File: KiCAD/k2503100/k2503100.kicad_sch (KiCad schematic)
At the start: 0 parts

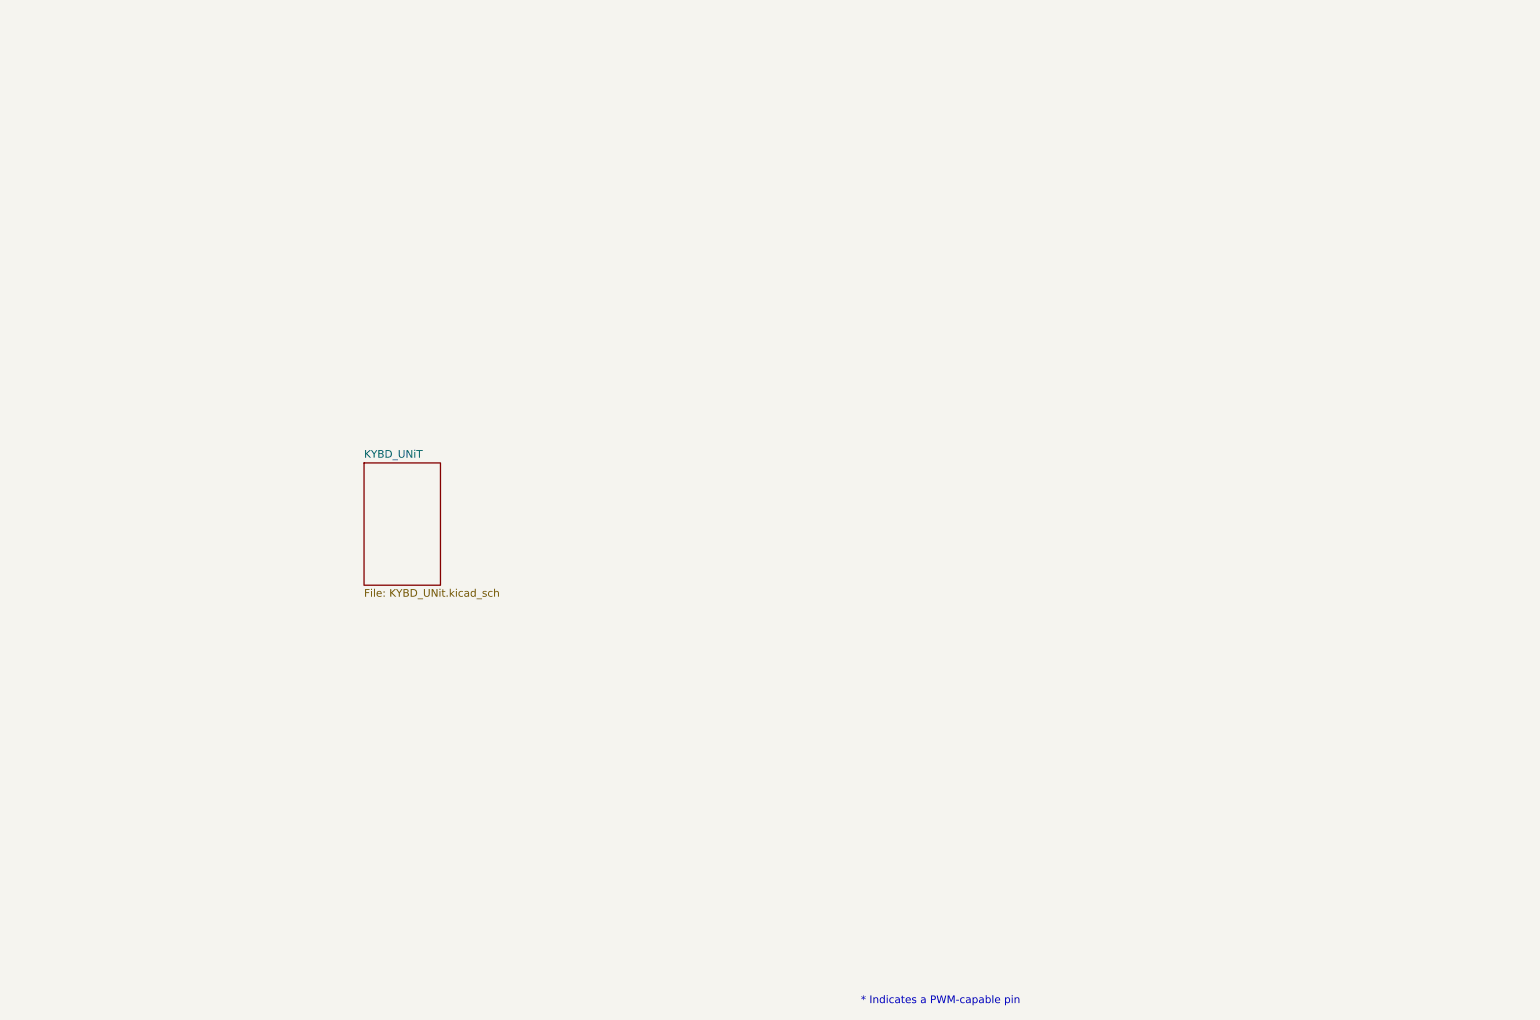
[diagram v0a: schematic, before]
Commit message: KCOL側配線途中
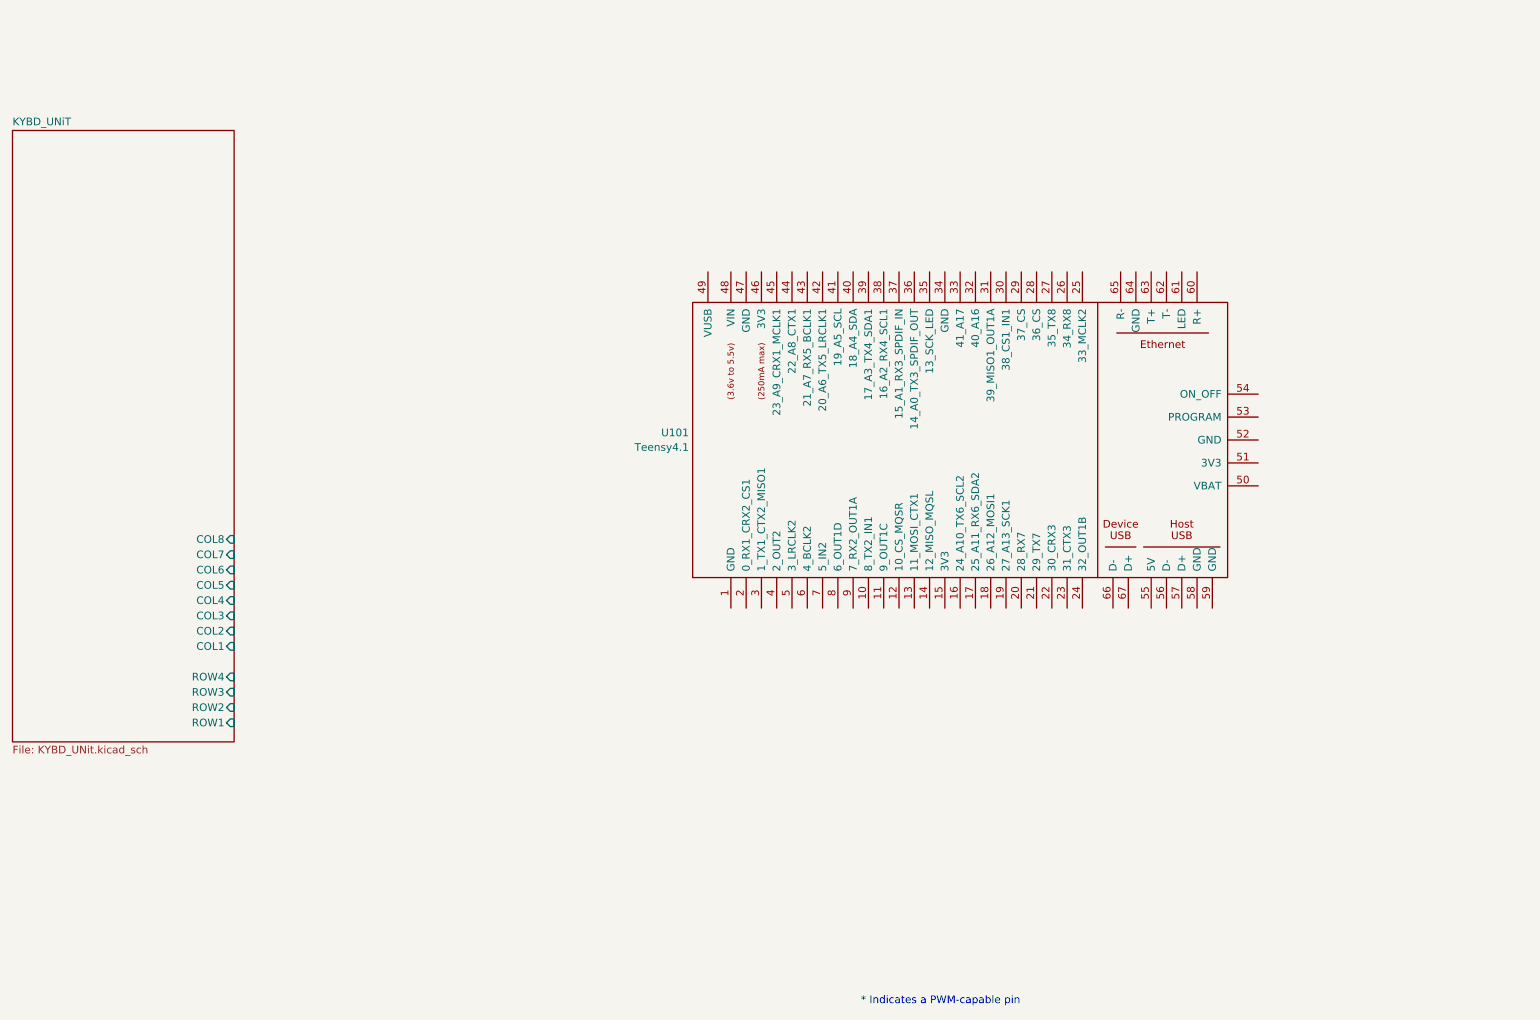
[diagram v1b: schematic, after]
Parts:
- added U101: Teensy4.1, symbol teensy:Teensy4.1
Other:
- sheet KYBD_UNiT ports: added COL1, COL2, COL3, COL4, COL5, COL6, COL7, COL8, ROW1, ROW2, ROW3, ROW4; removed none

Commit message: KYBD UNIT ほぼ完成
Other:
- sheet KYBD_UNiT ports: added KCOL1, KCOL2, KCOL3, KCOL4, KCOL5, KCOL6, KCOL7, KCOL8, KROW1, KROW2, KROW3, KROW4; removed none
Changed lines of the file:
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@@
 	)
 	(sheet
-		(at 36.83 34.925)
-		(size 36.83 101.6)
+		(at 36.83 61.595)
+		(size 36.83 74.93)
 		(fields_autoplaced yes)
 		(stroke
@@
 		)
 		(property "Sheetname" "KYBD_UNiT"
-			(at 36.83 34.2134 0)
+			(at 36.83 60.8834 0)
 			(effects
 				(font
@@
 		(pin "ROW1" input
 			(at 73.66 133.35 0)
+			(effects
+				(font
+					(size 1.27 1.27)
+				)
+				(justify right)
+			)
+		)
+		(pin "KCOL1" input
+			(at 73.66 96.52 0)
+			(effects
+				(font
+					(size 1.27 1.27)
+				)
+				(justify right)
+			)
+		)
+		(pin "KCOL2" input
+			(at 73.66 93.98 0)
+			(effects
+				(font
+					(size 1.27 1.27)
+				)
+				(justify right)
+			)
+		)
+		(pin "KCOL3" input
+			(at 73.66 91.44 0)
+			(effects
+				(font
+					(size 1.27 1.27)
+				)
+				(justify right)
+			)
+		)
+		(pin "KCOL4" input
+			(at 73.66 88.9 0)
+			(effects
+				(font
+					(size 1.27 1.27)
+				)
+				(justify right)
+			)
+		)
+		(pin "KCOL5" input
+			(at 73.66 86.36 0)
+			(effects
+				(font
+					(size 1.27 1.27)
+				)
+				(justify right)
+			)
+		)
+		(pin "KCOL6" input
+			(at 73.66 83.82 0)
+			(effects
+				(font
+					(size 1.27 1.27)
+				)
+				(justify right)
+			)
+		)
+		(pin "KCOL7" input
+			(at 73.66 81.28 0)
+			(effects
+				(font
+					(size 1.27 1.27)
+				)
+				(justify right)
+			)
+		)
+		(pin "KCOL8" input
+			(at 73.66 78.74 0)
+			(effects
+				(font
+					(size 1.27 1.27)
+				)
+				(justify right)
+			)
+		)
+		(pin "KROW3" input
+			(at 73.66 67.31 0)
+			(effects
+				(font
+					(size 1.27 1.27)
+				)
+				(justify right)
+			)
+		)
+		(pin "KROW4" input
+			(at 73.66 64.77 0)
+			(effects
+				(font
+					(size 1.27 1.27)
+				)
+				(justify right)
+			)
+		)
+		(pin "KROW2" input
+			(at 73.66 69.85 0)
+			(effects
+				(font
+					(size 1.27 1.27)
+				)
+				(justify right)
+			)
+		)
+		(pin "KROW1" input
+			(at 73.66 72.39 0)
 			(effects
 				(font
@@
 			(project "k2503100"
 				(path "/e63e39d7-6ac0-4ffd-8aa3-1841a4541b55"
-					(page "3")
-				)
-			)
+					(page "2")
+				)
+			)

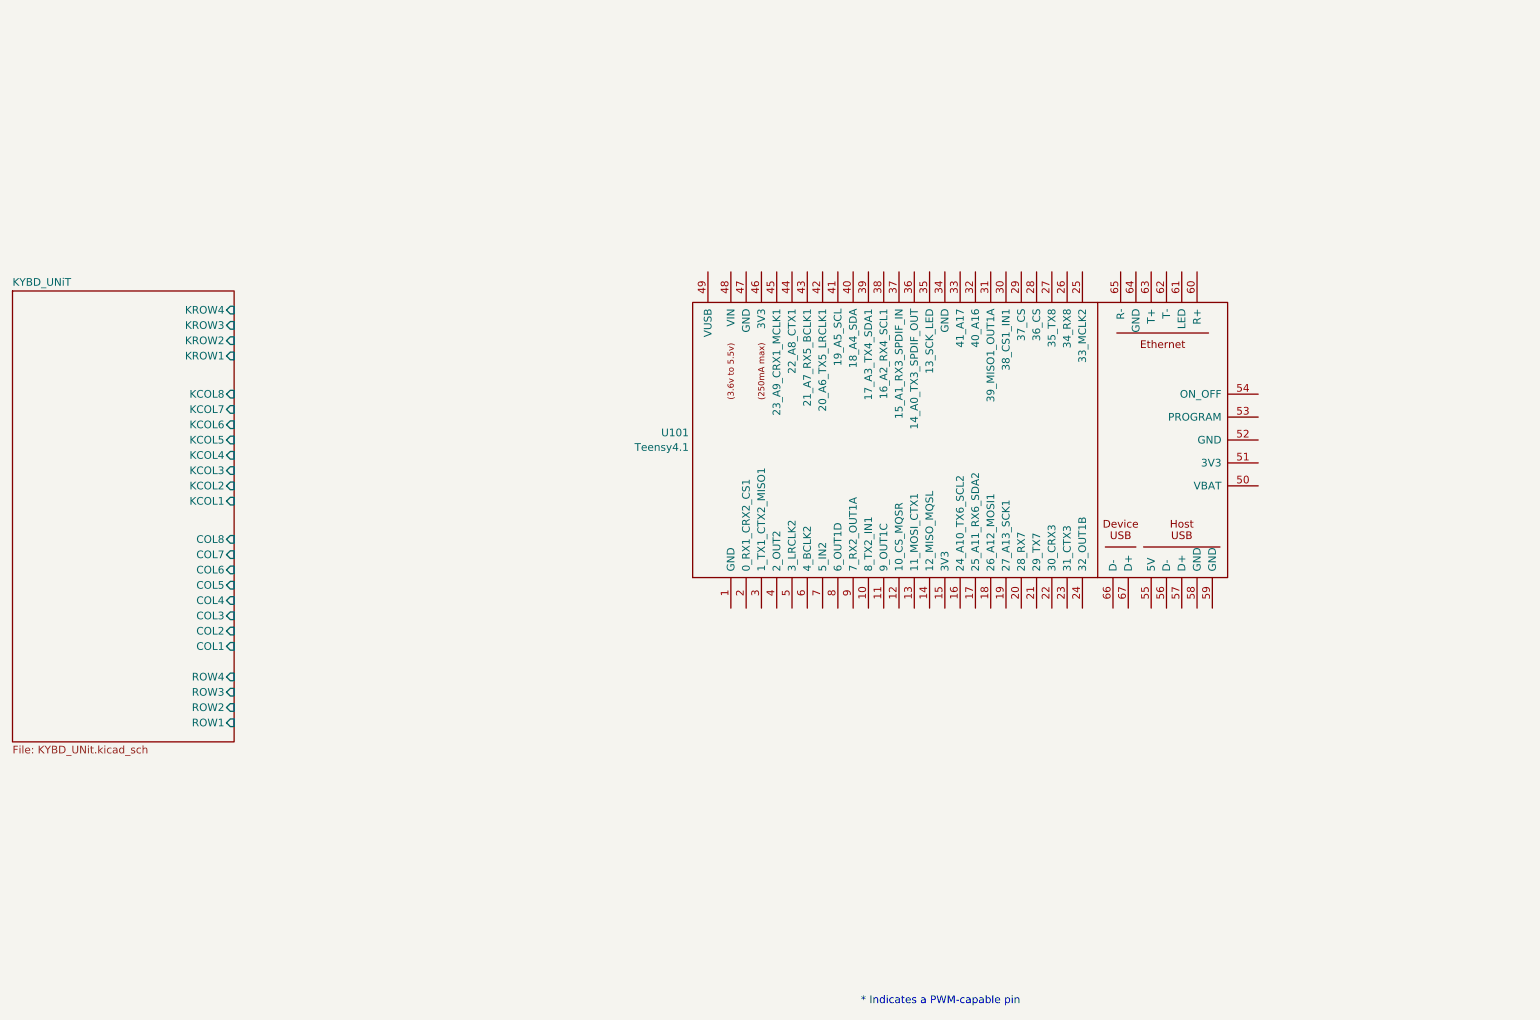
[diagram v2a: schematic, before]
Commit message: CPUとの接続途中
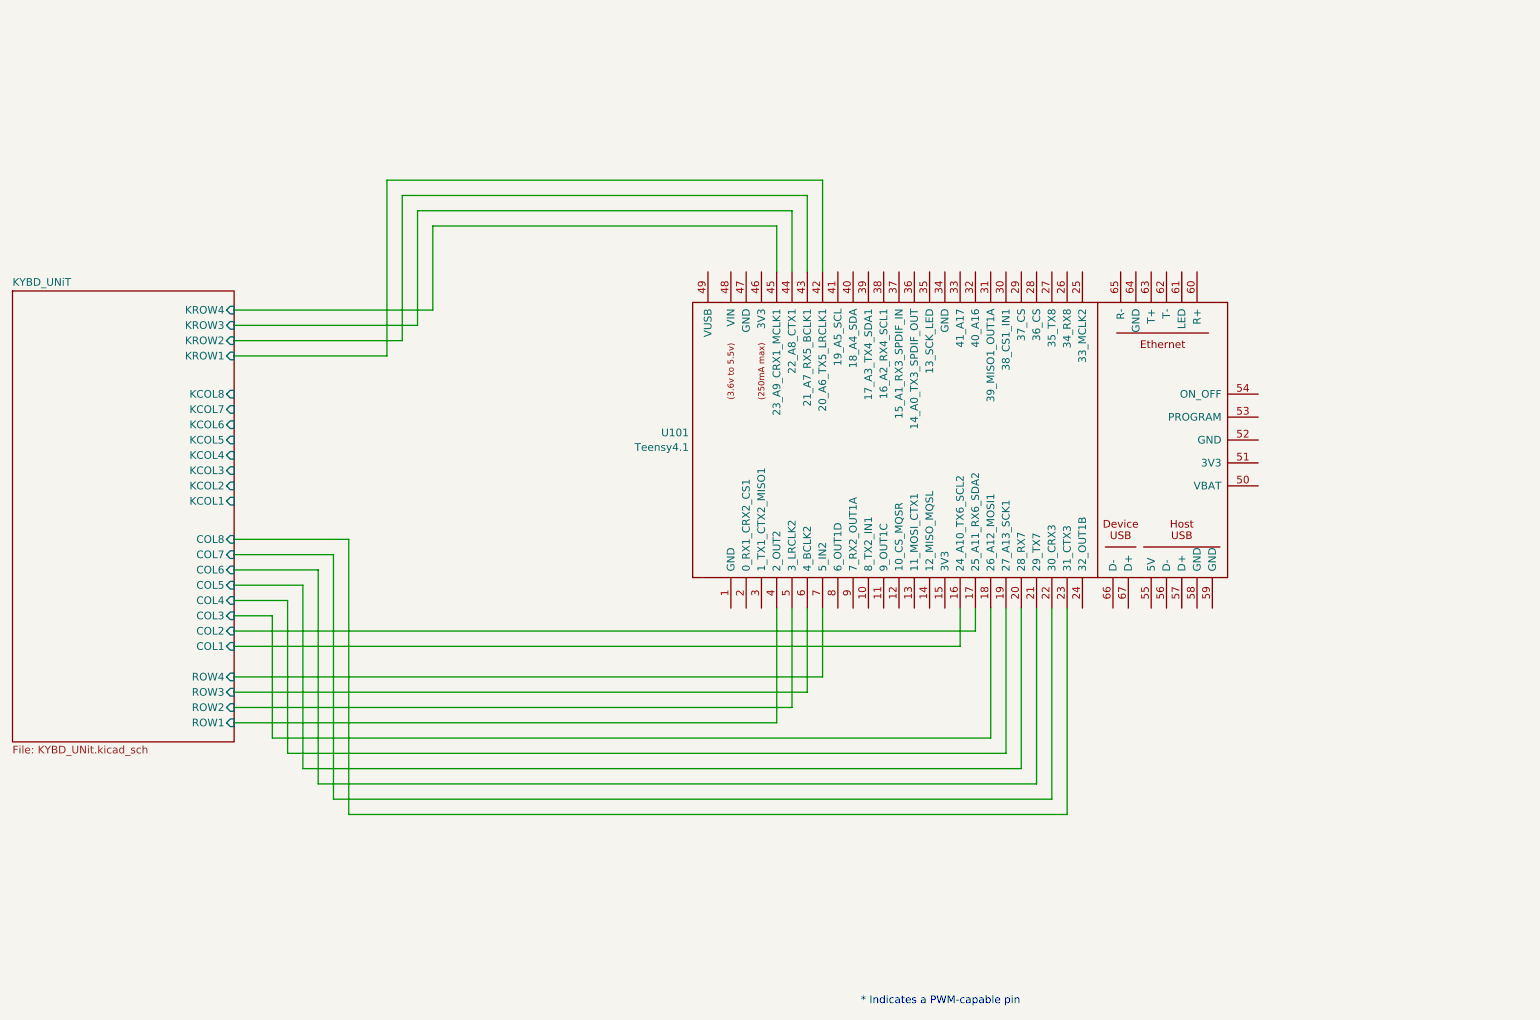
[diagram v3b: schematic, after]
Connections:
- net KYBD_UNiT/COL1: now also U101.16 (24_A10_TX6_SCL2)
- net KYBD_UNiT/COL2: now also U101.17 (25_A11_RX6_SDA2)
- net KYBD_UNiT/COL3: now also U101.18 (26_A12_MOSI1)
- net KYBD_UNiT/COL4: now also U101.19 (27_A13_SCK1)
- net KYBD_UNiT/COL5: now also U101.20 (28_RX7)
- net KYBD_UNiT/COL6: now also U101.21 (29_TX7)
- net KYBD_UNiT/COL7: now also U101.22 (30_CRX3)
- net KYBD_UNiT/COL8: now also U101.23 (31_CTX3)
- net KYBD_UNiT/KROW1: now also U101.42 (20_A6_TX5_LRCLK1)
- net KYBD_UNiT/KROW2: now also U101.43 (21_A7_RX5_BCLK1)
- net KYBD_UNiT/KROW3: now also U101.44 (22_A8_CTX1)
- net KYBD_UNiT/KROW4: now also U101.45 (23_A9_CRX1_MCLK1)
- net KYBD_UNiT/ROW1: now also U101.4 (2_OUT2)
- net KYBD_UNiT/ROW2: now also U101.5 (3_LRCLK2)
- net KYBD_UNiT/ROW3: now also U101.6 (4_BCLK2)
- net KYBD_UNiT/ROW4: now also U101.7 (5_IN2)

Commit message: PDF作成
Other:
- company: (none) -> HOLLY&Co.,Ltd. Masafumi Horimoto
- title: (none) -> k2503100 操作パネル
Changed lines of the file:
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@@
 	(paper "A4")
 	(title_block
-		(date "mar. 31 mars 2015")
+		(title "k2503100 操作パネル")
+		(date "2024-10-02")
+		(rev "0.90")
+		(company "HOLLY&Co.,Ltd. Masafumi Horimoto")
 	)
 	(wire
@@
 	(text "* Indicates a PWM-capable pin"
 		(exclude_from_sim no)
-		(at 177.8 180.34 0)
+		(at 251.968 179.832 0)
 		(effects
 			(font

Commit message: 途中
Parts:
- added SW1, SW2, SW3: SW_Push, symbol Switch:SW_Push
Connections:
- net KYBD_UNiT/KCOL1: now also U101.25 (33_MCLK2)
- net KYBD_UNiT/KCOL2: now also U101.26 (34_RX8)
- net KYBD_UNiT/KCOL3: now also U101.27 (35_TX8)
- net KYBD_UNiT/KCOL4: now also U101.28 (36_CS)
- net KYBD_UNiT/KCOL5: now also U101.29 (37_CS)
- net KYBD_UNiT/KCOL6: now also U101.30 (38_CS1_IN1)
- net KYBD_UNiT/KCOL7: now also U101.31 (39_MISO1_OUT1A)
- net KYBD_UNiT/KCOL8: now also U101.32 (40_A16)
- net at U101.34 (GND): now also SW1.1, SW2.1, SW3.1
- net at U101.36 (14_A0_TX3_SPDIF_OUT): now also SW1.2
- net at U101.37 (15_A1_RX3_SPDIF_IN): now also SW2.2
- net at U101.38 (16_A2_RX4_SCL1): now also SW3.2
- no-connect marks 0 -> 25

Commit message: PCBデザイン開始
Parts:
- SW1, SW2, SW3: footprint (none) -> HOLLY2:MP86A1
- U101: footprint (none) -> teensy:Teensy41
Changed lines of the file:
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@@
 			)
 		)
-		(property "Footprint" ""
+		(property "Footprint" "HOLLY2:MP86A1"
 			(at 76.2 24.13 0)
 			(effects
@@
 			)
 		)
-		(property "Footprint" ""
+		(property "Footprint" "HOLLY2:MP86A1"
 			(at 76.2 15.24 0)
 			(effects
@@
 			)
 		)
-		(property "Footprint" ""
+		(property "Footprint" "HOLLY2:MP86A1"
 			(at 76.2 33.02 0)
 			(effects
@@
 			)
 		)
-		(property "Footprint" ""
+		(property "Footprint" "teensy:Teensy41"
 			(at 200.66 96.52 0)
 			(effects

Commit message: PCB設計中
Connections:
- net GND: now reaches SW1.1, SW2.1, SW3.1, U101.34 (GND)
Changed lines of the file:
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@@
+		)
+	)
+	(label "GND"
+		(at 190.5 53.34 0)
+		(effects
+			(font
+				(size 1.27 1.27)
+			)
+			(justify left bottom)
 		)
 	)
